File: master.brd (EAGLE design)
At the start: 160 x 100 mm, 27 parts, among them IC1 MEGA164/324/644/1284, SW1 CI-11, U2 3V3 something

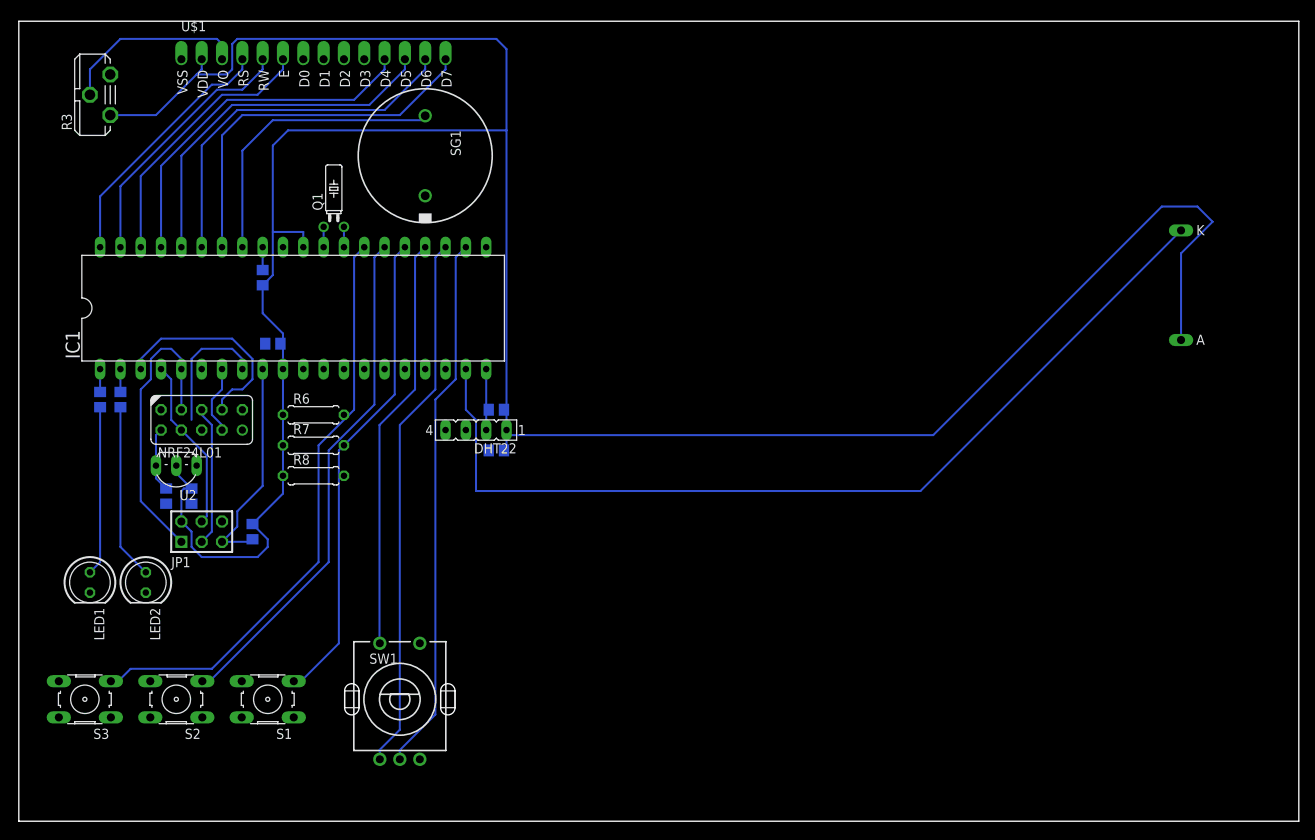
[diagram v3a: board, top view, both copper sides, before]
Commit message: added forgotten lan interface
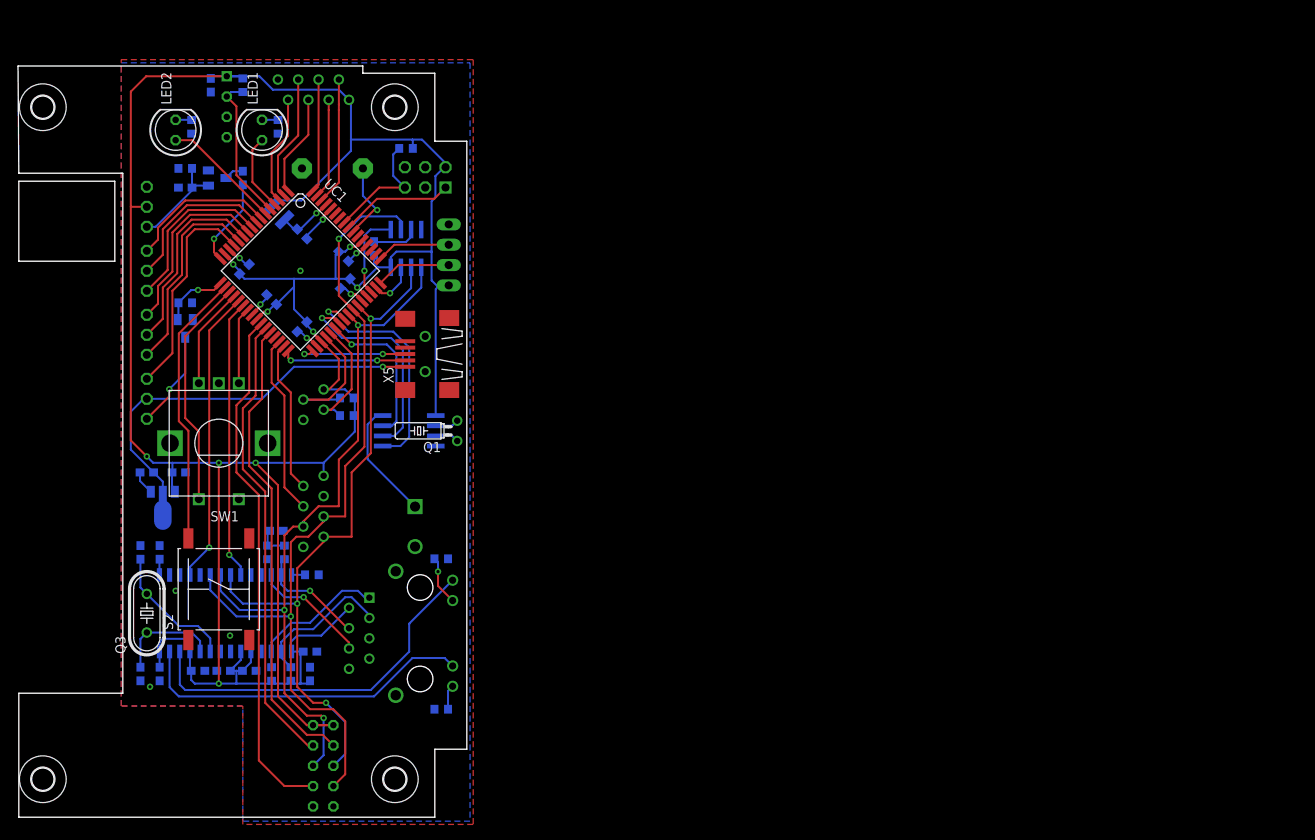
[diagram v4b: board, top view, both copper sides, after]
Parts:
- removed DHT22: (no value), con-lsta:FE04-1
- removed JP1: AVR-ISP-6VERT, avr-7:AVR-ISP-6
- removed NRF24L01: (no value), con-lsta:FE05-2
- removed S1, S3: (no value), switch-omron:B3F-10XX
- removed U$1: BTHQ24008VSS, lcd_displays:BTHQ42008VSS
- removed U2: 3V3 something, asko:TO92-LOWDROP
- added C10, C11, C12, C17, C18, C19, C20, C21, C4, C5, C6, C9: 100n, rcl:C0603
- added C13, C15: 10n, rcl:C0603
- added C14: .22, carrilib:SUPERCAP
- added C16: 10u, rcl:C0603
- added C22, C23: 22p, rcl:C0603
- added D1: BAS40-04, diode:SOT23
- added IC2: MCP1703-3302, karlnet-parts:SOT89
- added IC3: ENC28J60SO, microchip:SO28W
- added L2: 10u, inductor-neosid:SM-NE29
- added LAN1: MAGJACK, magjack:MAGJACK
- added M1: DHT22-NP, modules:DHT22-NOPRINT
- added M2: NRF24L01P-M, modules:NRF24L01P-A
- added PDI: AVR-PDIVERT, avr-7:AVR-ISP-6
- added Q2: IRLML2502, mosfet:MICRO3
- added Q3: 25MHz, crystal:HC49/S
- added R10, R12: 49R9, rcl:R0603
- added R11: 4k7, rcl:R0603
- added R13: 2k, rcl:R0603
- added R14, R15: 100, rcl:R0603
- added R9: 10K, rcl:R0603
- added U$3, U$4, U$5, U$6: (no value), holes:2,8
- added U1: 25LC640A-E/SN, microchip:SOIC127P600X175-8N
- added UC1: XMEGA-A3TQFP, avr-7:TQFP64
- added X1: serial, pinhead-mod:1X04
- added X2: SPI/1W, con-amp-micromatch:MICROMATCH-8
- added X3: I2C, con-amp-micromatch:MICROMATCH-4
- added X4: ADC, con-amp-micromatch:MICROMATCH-8
- added X5: (no value), con-usb:USB-MB-S
- added X6, X7, X8, X9: PS25_3W-R, con_PS25:PS25_3
- C1, C2, C3, C7, C8: device rcl:C0805 -> rcl:C0603
- IC1: value MEGA164/324/644/1284 -> DS1302SOIC; device avr-7:DIL40 -> adafruit:SOIC8_208MIL
- R1, R2, R4, R5: device rcl:R0805 -> rcl:R0603
- R3: value 10k -> 10K; device pot:ST10 -> rcl:R0603
- R6, R7: value 4k7 -> 49R9; device rcl:0207/7 -> rcl:R0603
- R8: device rcl:0207/7 -> rcl:R0603
- S2: device switch-omron:B3F-10XX -> jt-switches:MEC-SMT
- SG1: value EFBAA40D101 -> RMP-14SP; device buzzer:EFBAA40D101 -> buzzer:F/CM12P
- SW1: value CI-11 -> EC12E_SW; device piher:CI-11 -> switch-alps:ALPS_EC12E_SW
- moved LED1 60.5 mm to (30.4, 86.4), turned to 90 degrees
- moved LED2 56.7 mm to (19.6, 86.4), turned to 90 degrees
- moved R1 51.6 mm to (48.4, 84.1), turned to 180 degrees
- moved R2 51.5 mm to (28.0, 92.0), turned to 90 degrees
- moved R4 40.7 mm to (32.4, 86.8)
- moved SW1 39.2 mm to (25.0, 47.2), turned to 180 degrees
- moved R5 35.2 mm to (21.6, 86.8)
- moved R6 32.5 mm to (34.0, 18.4), flipped to the bottom, turned to 90 degrees
- moved Q1 29.8 mm to (54.8, 48.8), turned to 90 degrees
- moved R7 29.1 mm to (31.6, 18.4), flipped to the bottom, turned to 90 degrees
- moved C3 28.8 mm to (35.4, 61.8), turned to 315 degrees
- moved IC1 21.1 mm to (48.8, 48.8), flipped to the bottom, turned to 270 degrees
- moved S2 14.8 mm to (25.0, 29.0), turned to 90 degrees
- moved R3 14.1 mm to (20.8, 81.6), flipped to the bottom, turned to 180 degrees
- moved SG1 11.7 mm to (39.2, 81.6), flipped to the bottom, turned to 180 degrees
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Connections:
- removed net !RESET: IC1.9, JP1.5, R1.1
- removed net +3V3: C8.1, NRF24L01.10, NRF24L01.9, U2.OUT
- removed net PA0: IC1.40, U$1.RS
- removed net PA1: IC1.39, U$1.RW
- removed net PA2: IC1.38, U$1.E
- removed net PA3: IC1.37, U$1.D4
- removed net PA4: IC1.36, U$1.D5
- removed net PA5: IC1.35, U$1.D6
- removed net PA6: IC1.34, U$1.D7
- removed net PA7: IC1.33, SG1.1
- removed net PB0: IC1.1, R4.1
- removed net PB1: IC1.2, R5.1
- removed net PB2: IC1.3, NRF24L01.4
- removed net PB3: IC1.4, JP1.4, NRF24L01.7
- removed net PB4: IC1.5, JP1.1, NRF24L01.8
- removed net PB5: IC1.6, JP1.3, R8.2
- removed net PB6: IC1.7, R7.1
- removed net PB7: IC1.8, R6.1
- removed net PC0: IC1.22, SW1.B
- removed net PC1: IC1.23, SW1.A
- removed net PC2: IC1.24, SW1.D
- removed net PC3: IC1.25, S1.3
- removed net PC4: IC1.26, S2.3
- removed net PC5: IC1.27, S3.3
- removed net PD5: IC1.19, U$1.K
- removed net PD6: DHT22.2, IC1.20, R2.2
- new net !EEPCS: U1.1, UC1.46
- new net !EEPHOLD: U1.7, UC1.47
- new net !LANCS: IC3.9, UC1.22
- new net !LANINT: IC3.4, UC1.21
- new net !RFCS: M2.CSN, UC1.27
- new net ADC0: UC1.62, X4.2
- new net ADC1: UC1.63, X4.3
- new net ADC2: UC1.64, X4.4
- new net ADC3: UC1.1, X4.5
- new net ADC4: UC1.2, X4.6
- new net ADC5: UC1.3, X4.7
- new net BUZZ: SG1.+, UC1.55
- new net DHTDATA: M1.2, R2.1, UC1.5
- new net LCD_BGLED: Q2.1, R9.1, UC1.17
- new net LCD_CONTR: C11.1, UC1.16
- new net LCD_D4: UC1.10, X8.1
- new net LCD_D5: UC1.11, X8.2
- new net LCD_D6: UC1.12, X8.3
- new net LCD_D7: UC1.13, X9.1
- new net LCD_E: UC1.9, X7.3
- new net LCD_RS: UC1.7, X7.1
- new net LCR_RW: UC1.8, X7.2
- new net LED1: LED1.A, UC1.4
- new net LED2: LED2.A, UC1.6
- new net MISO: IC3.6, M2.MISO, U1.2, UC1.42, X2.5
- new net MOSI: IC3.7, M2.MOSI, U1.5, UC1.41, X2.6
- new net N$10: PDI.1, UC1.56
- new net N$11: PDI.5, R1.1, UC1.57
- new net N$12: IC3.12, LAN1.6, R12.1
- new net N$14: IC3.17, LAN1.1, R7.2
- new net N$15: C6.1, L2.1, UC1.61
- new net N$16: C15.1, R10.2, R12.2
- new net N$17: IC3.14, R13.1
- new net N$18: C23.1, IC3.24, Q3.1
- new net N$19: C22.1, IC3.23, Q3.2
- new net N$20: C16.1, IC3.1
- new net N$21: IC3.27, LAN1.LED2.1
- new net N$22: IC3.26, LAN1.LED1.1
- new net N$23: LAN1.LED2.2, R14.1
- new net N$24: LAN1.LED1.2, R15.1
- new net N$8: Q2.3, X9.3
- new net RFCE: M2.CE, UC1.28
- new net RFIRQ: M2.IRQ, UC1.26
- new net RTC_CE: IC1.5, UC1.40
- new net RTC_CLK: IC1.7, UC1.38
- new net RTC_IO: IC1.6, UC1.39
- new net RXD: UC1.48, X1.2
- new net S1A: SW1.A, UC1.23
- new net S1B: SW1.B, UC1.20
- new net S1P: SW1.E, UC1.19
- new net S2: S2.1, UC1.18
- new net SCK: IC3.8, M2.SCK, U1.6, UC1.43, X2.7
- new net SCL: R11.2, UC1.37, X3.3
- new net SDA: R8.2, UC1.36, X3.2
- new net SS1WA: UC1.31, X2.2
- new net SS1WB: UC1.30, X2.4
- new net TXD: UC1.49, X1.3
- new net USBD_N: UC1.32, X5.D-
- new net USBD_P: UC1.33, X5.D+
- new net VCC: C1.1, C12.1, C13.1, C17.1, C18.1, C19.1, C2.1, C20.1, C21.1, C3.1, C4.1, C5.1, C8.1, C9.2, IC1.1, IC2.3, IC3.15, IC3.19, IC3.20, IC3.25, IC3.28, L2.2, LAN1.2, M1.1, M2.VCC_A, M2.VCC_B, PDI.2, R1.2, R11.1, R2.2, R6.1, R7.1, R8.1, U1.8, UC1.15, UC1.25, UC1.35, UC1.45, UC1.53, X1.1, X2.1, X3.1, X4.1, X6.2
- net +5V: now also IC2.2, IC2.2@1, X5.VBUS, X9.2; no longer C1.1, C2.1, C3.2, DHT22.1, IC1.10, IC1.30, JP1.2, R1.2, R2.1, R3.A, U$1.A, U$1.VDD, U2.IN
- net GND: now also C10.1, C12.2, C13.2, C14.P$2, C15.2, C16.2, C17.2, C18.2, C19.2, C2.2, C20.2, C21.2, C22.2, C23.2, C3.2, C4.2, C5.2, C6.2, C9.1, D1.2, IC1.4, IC2.1, IC3.11, IC3.18, IC3.2, IC3.21, IC3.22, LAN1.8, M1.4, M2.GND_A, M2.GND_B, PDI.6, Q2.2, R13.2, R14.2, R15.2, R3.1, R4.2, R5.2, R9.2, S2.3, S2.4, SG1.-, SW1.D, U1.3, U1.4, UC1.14, UC1.24, UC1.34, UC1.44, UC1.52, UC1.60, X1.4, X2.3, X2.8, X3.4, X4.8, X5.GND, X6.1; no longer C3.1, DHT22.4, IC1.11, IC1.31, JP1.6, LED1.K, LED2.K, NRF24L01.1, NRF24L01.2, R3.E, S1.1, S1.2, S2.1, S2.2, S3.1, S3.2, SG1.2, SW1.E, U$1.VSS, U2.GND
- net N$1: now also IC1.2, Q1.2; no longer C2.2, IC1.32
- net N$13: now also IC3.16, LAN1.3, R6.2; no longer LED1.A, R4.2
- net N$2: now also LED1.K, R4.1; no longer LED2.A, R5.2
- net N$3: now also IC1.3; no longer IC1.29
- net N$4: now also C11.2, D1.3; no longer IC1.28, Q1.2
- net N$5: now also LED2.K, R5.1; no longer NRF24L01.5, R6.2
- net N$6: now also C14.P$1, IC1.8; no longer NRF24L01.3, R7.2
- net N$7: now also IC3.13, LAN1.4, R10.1; no longer NRF24L01.6, R8.1
- net N$9: now also C10.2, D1.1, R3.2, X6.3; no longer R3.S, U$1.VO
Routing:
- net VCC: track 0.00 -> 378.0 mm, vias 0 -> 9
- net +5V: track 339.6 -> 51.2 mm, vias 0 -> 1
- net PD5: track 117.4 -> 0.00 mm
- net MISO: track 0.00 -> 104.7 mm, vias 0 -> 2
- net MOSI: track 0.00 -> 89.9 mm, vias 0 -> 3
- net SCK: track 0.00 -> 88.4 mm, vias 0 -> 3
- net PC5: track 73.9 -> 0.00 mm
- net PC0: track 67.4 -> 0.00 mm
- net PC1: track 67.4 -> 0.00 mm
- net RFIRQ: track 0.00 -> 65.1 mm
- net PC4: track 64.2 -> 0.00 mm
- net PC3: track 60.5 -> 0.00 mm
- net RFCE: track 0.00 -> 58.2 mm
- net !RFCS: track 0.00 -> 57.4 mm
- net PC2: track 51.9 -> 0.00 mm
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- added copper zone on layer 1, net GND
- added copper zone on layer 16, net GND
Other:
- board size 160 x 100 mm -> 56.1 x 93.9 mm

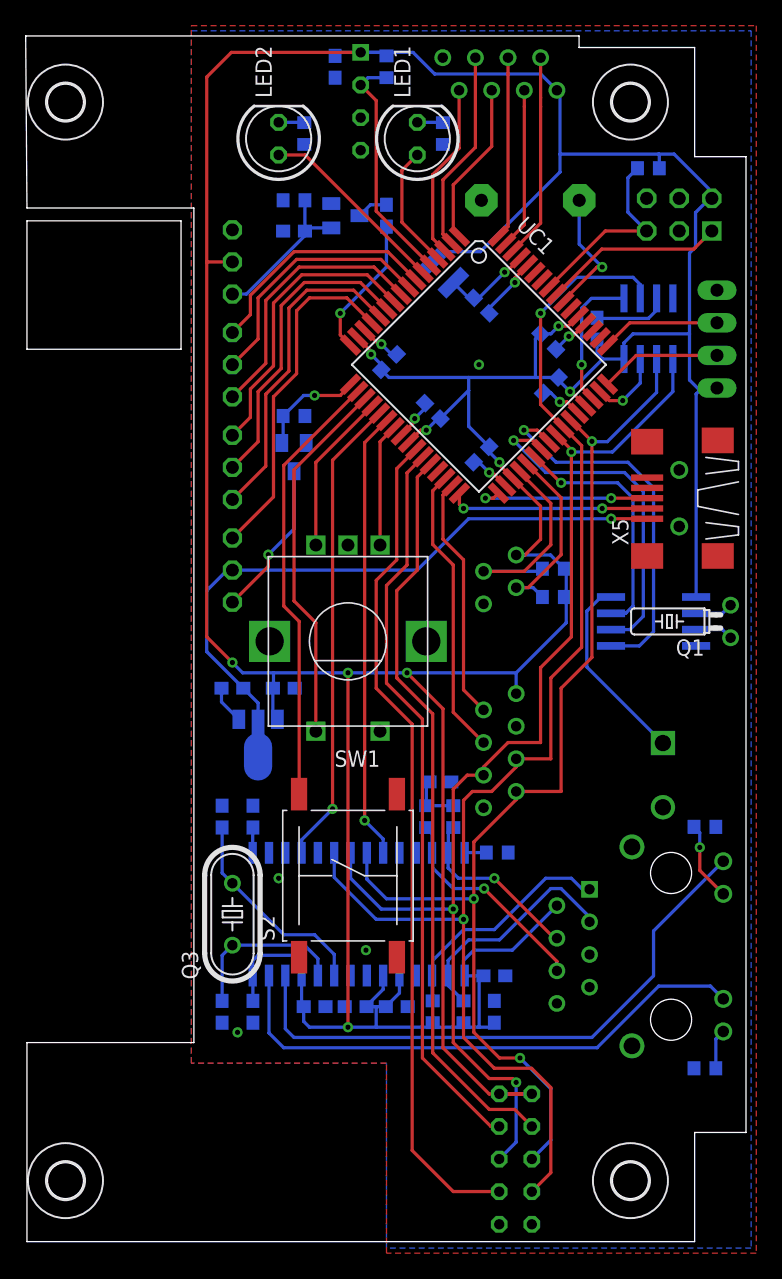
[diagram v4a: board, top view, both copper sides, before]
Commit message: improved spacing between some layers
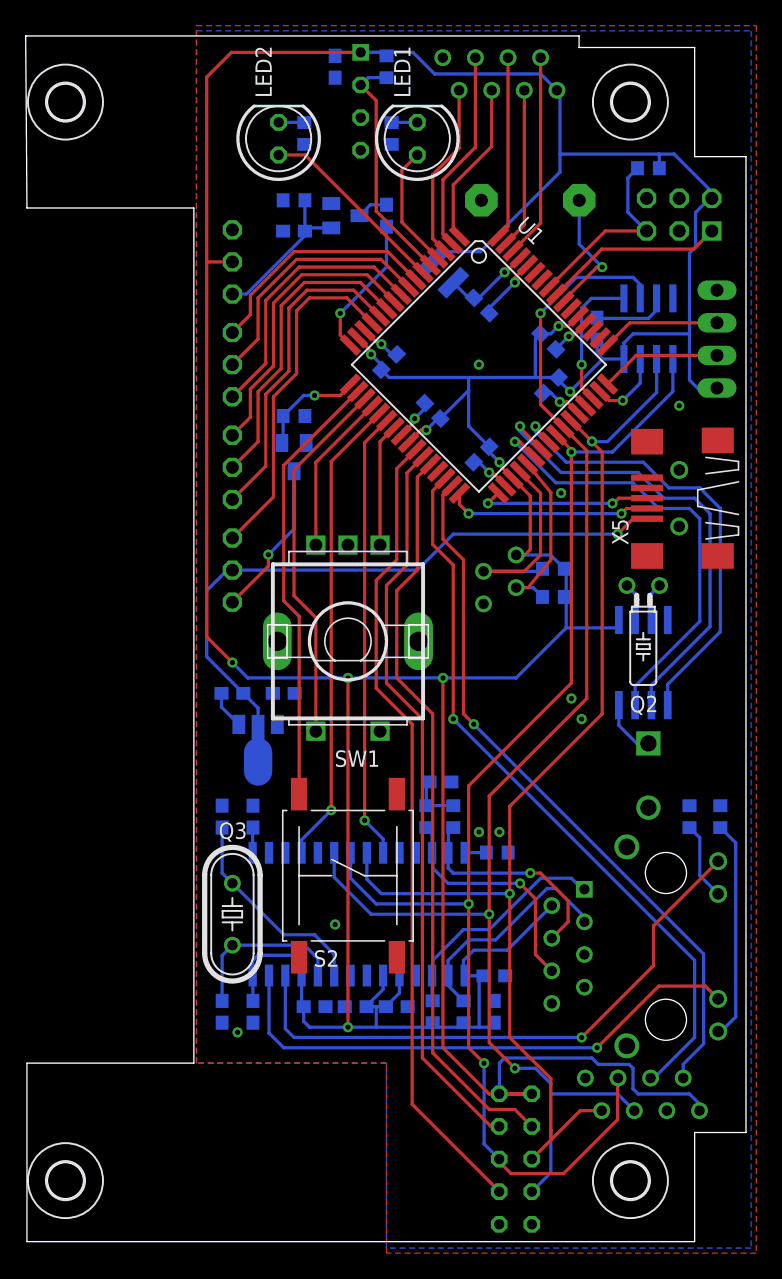
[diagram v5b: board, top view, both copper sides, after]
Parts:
- removed IC1: DS1302SOIC, adafruit:SOIC8_208MIL
- removed UC1: XMEGA-A3TQFP, avr-7:TQFP64
- added U2: DS1302SOIC, adafruit:SOIC8_208MIL
- added U3: 25LC640A-E/SN, microchip:SOIC127P600X175-8N
- Q1: value (none) -> IRLML2502; device crystal:TC26H -> mosfet:MICRO3
- Q2: value IRLML2502 -> (none); device mosfet:MICRO3 -> crystal:TC26H
- SW1: value EC12E_SW -> EC11E_SW; device switch-alps:ALPS_EC12E_SW -> switch-alps:ALPS_EC11E_SW
- U1: value 25LC640A-E/SN -> XMEGA-A3TQFP; device microchip:SOIC127P600X175-8N -> avr-7:TQFP64
- moved Q1 36.3 mm to (20.8, 61.6), flipped to the bottom, turned to 180 degrees
- moved Q2 29.0 mm to (48.0, 51.6), flipped to the top
- moved X2 29.0 mm to (47.9, 12.0), turned to 180 degrees
- moved R14 19.6 mm to (54.0, 33.6), turned to 90 degrees
- moved U1 13.5 mm to (35.2, 68.8), flipped to the top, turned to 315 degrees
- moved R4 4.00 mm to (28.4, 86.8)
- moved R15 1.44 mm to (51.6, 33.6), turned to 90 degrees
- moved C14 1.13 mm to (48.4, 36.8)
- moved IC2 0.40 mm to (18.0, 38.8)
- moved C7 0.40 mm to (16.0, 43.2)
- moved C8 0.40 mm to (20.0, 43.2)
- moved LAN1 0.40 mm to (49.8, 23.5)
- renumbered IC3 to U4, L2 to L1
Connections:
- net !EEPCS: now also U1.46, U3.1; no longer U1.1, UC1.46
- net !EEPHOLD: now also U1.47, U3.7; no longer U1.7, UC1.47
- net !LANCS: now also U1.22; no longer UC1.22
- net !LANINT: now also U1.21; no longer UC1.21
- net !RFCS: now also U1.27; no longer UC1.27
- net ADC0: now also U1.62; no longer UC1.62
- net ADC1: now also U1.63; no longer UC1.63
- net ADC2: now also U1.64; no longer UC1.64
- net ADC3: now also U1.1; no longer UC1.1
- net ADC4: now also U1.2; no longer UC1.2
- net ADC5: now also U1.3; no longer UC1.3
- net BUZZ: now also U1.55; no longer UC1.55
- net DHTDATA: now also U1.5; no longer UC1.5
- net GND: now also Q1.2, SW1.GND1, SW1.GND2, U1.14, U1.24, U1.34, U1.44, U1.52, U1.60, U2.4, U3.3, U3.4; no longer IC1.4, Q2.2, U1.3, U1.4, UC1.14, UC1.24, UC1.34, UC1.44, UC1.52, UC1.60
- net LCD_BGLED: now also Q1.1, U1.17; no longer Q2.1, UC1.17
- net LCD_CONTR: now also U1.16; no longer UC1.16
- net LCD_D4: now also U1.10; no longer UC1.10
- net LCD_D5: now also U1.11; no longer UC1.11
- net LCD_D6: now also U1.12; no longer UC1.12
- net LCD_D7: now also U1.13; no longer UC1.13
- net LCD_E: now also U1.9; no longer UC1.9
- net LCD_RS: now also U1.7; no longer UC1.7
- net LCR_RW: now also U1.8; no longer UC1.8
- net LED1: now also U1.4; no longer UC1.4
- net LED2: now also U1.6; no longer UC1.6
- net MISO: now also U1.42, U3.2; no longer U1.2, UC1.42
- net MOSI: now also U1.41, U3.5; no longer U1.5, UC1.41
- net N$1: now also Q2.2, U2.2; no longer IC1.2, Q1.2
- net N$10: now also U1.56; no longer UC1.56
- net N$11: now also U1.57; no longer UC1.57
- net N$15: now also U1.61; no longer UC1.61
- net N$3: now also Q2.1, U2.3; no longer IC1.3, Q1.1
- net N$6: now also U2.8; no longer IC1.8
- net N$8: now also Q1.3; no longer Q2.3
- net RFCE: now also U1.28; no longer UC1.28
- net RFIRQ: now also U1.26; no longer UC1.26
- net RTC_CE: now also U1.40, U2.5; no longer IC1.5, UC1.40
- net RTC_CLK: now also U1.38, U2.7; no longer IC1.7, UC1.38
- net RTC_IO: now also U1.39, U2.6; no longer IC1.6, UC1.39
- net RXD: now also U1.48; no longer UC1.48
- net S1A: now also U1.23; no longer UC1.23
- net S1B: now also U1.20; no longer UC1.20
- net S1P: now also U1.19; no longer UC1.19
- net S2: now also U1.18; no longer UC1.18
- net SCK: now also U1.43, U3.6; no longer U1.6, UC1.43
- net SCL: now also U1.37; no longer UC1.37
- net SDA: now also U1.36; no longer UC1.36
- net SS1WA: now also U1.31; no longer UC1.31
- net SS1WB: now also U1.30; no longer UC1.30
- net TXD: now also U1.49; no longer UC1.49
- net USBD_N: now also U1.32; no longer UC1.32
- net USBD_P: now also U1.33; no longer UC1.33
- net VCC: now also U1.15, U1.25, U1.35, U1.45, U1.53, U2.1, U3.8; no longer IC1.1, U1.8, UC1.15, UC1.25, UC1.35, UC1.45, UC1.53
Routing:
- net SS1WA: track 19.1 -> 55.5 mm, vias 0 -> 1
- net SS1WB: track 22.6 -> 57.1 mm, vias 0 -> 1
- net RTC_CLK: track 19.3 -> 35.5 mm
- net N$23: track 3.11 -> 17.1 mm
- net N$6: track 15.1 -> 4.60 mm
- net MOSI: track 89.9 -> 100.4 mm
- net RTC_IO: track 26.9 -> 37.2 mm
- net RTC_CE: track 29.3 -> 36.0 mm
- net VCC: track 378.0 -> 383.5 mm
- net MISO: track 104.7 -> 109.0 mm, vias 2 -> 3
- net N$7: track 14.1 -> 17.2 mm
- net SCK: track 88.4 -> 91.3 mm, vias 3 -> 2
- net RFIRQ: track 65.1 -> 63.1 mm
- net N$12: track 16.8 -> 18.5 mm
- net SCL: track 15.1 -> 14.2 mm
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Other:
- outline, holes or cut-outs redrawn
